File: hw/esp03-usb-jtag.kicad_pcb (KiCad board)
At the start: 2 copper layers, 92.7 x 55.9 mm, 45 parts, among them J1 USB, P1 JTAG, P2 SERIAL, P3 CONN_2, SW1 POWER/RESET, SW2 STRAP, U1 ESP8266-ESP03, U2 FT2232H, U3 LM1117, U4 93LC46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

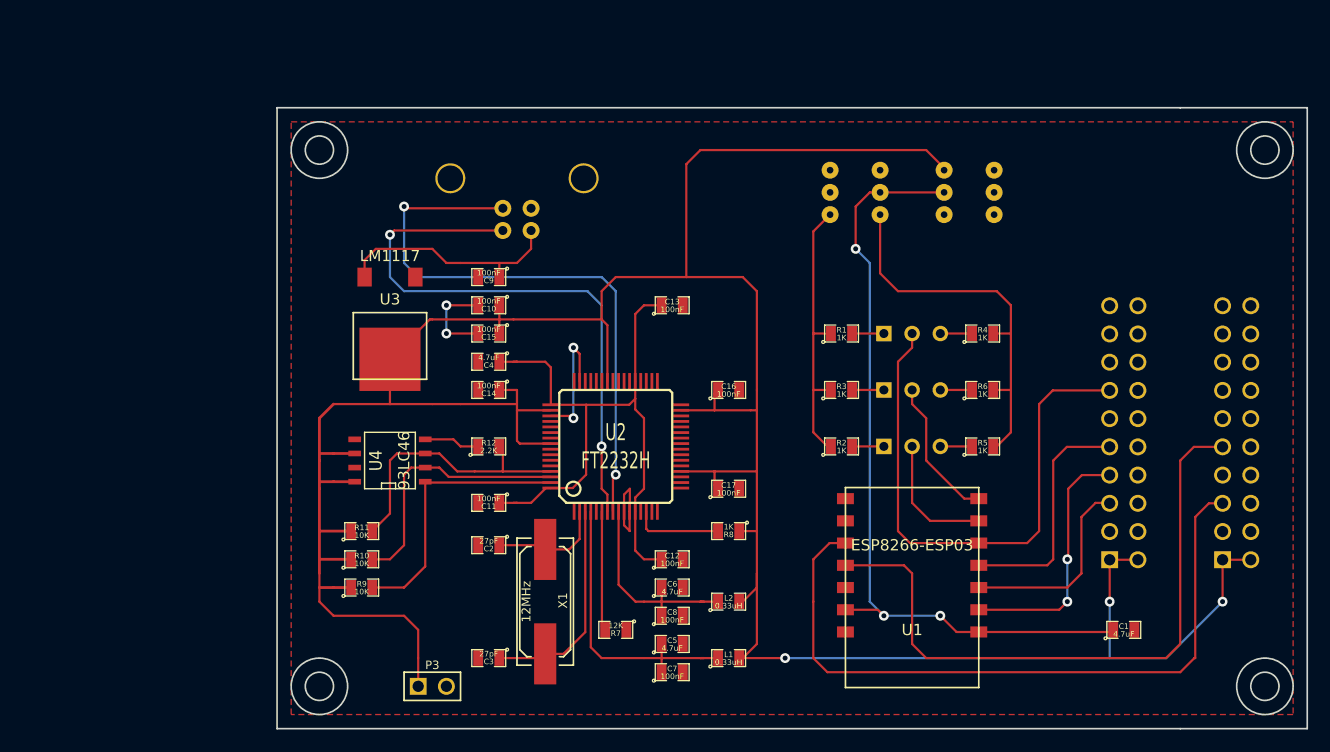
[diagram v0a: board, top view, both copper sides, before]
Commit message: hw: update PCB with FTDI JTAG and UART
Signed-off-by: Max Filippov <jcmvbkbc@gmail.com>
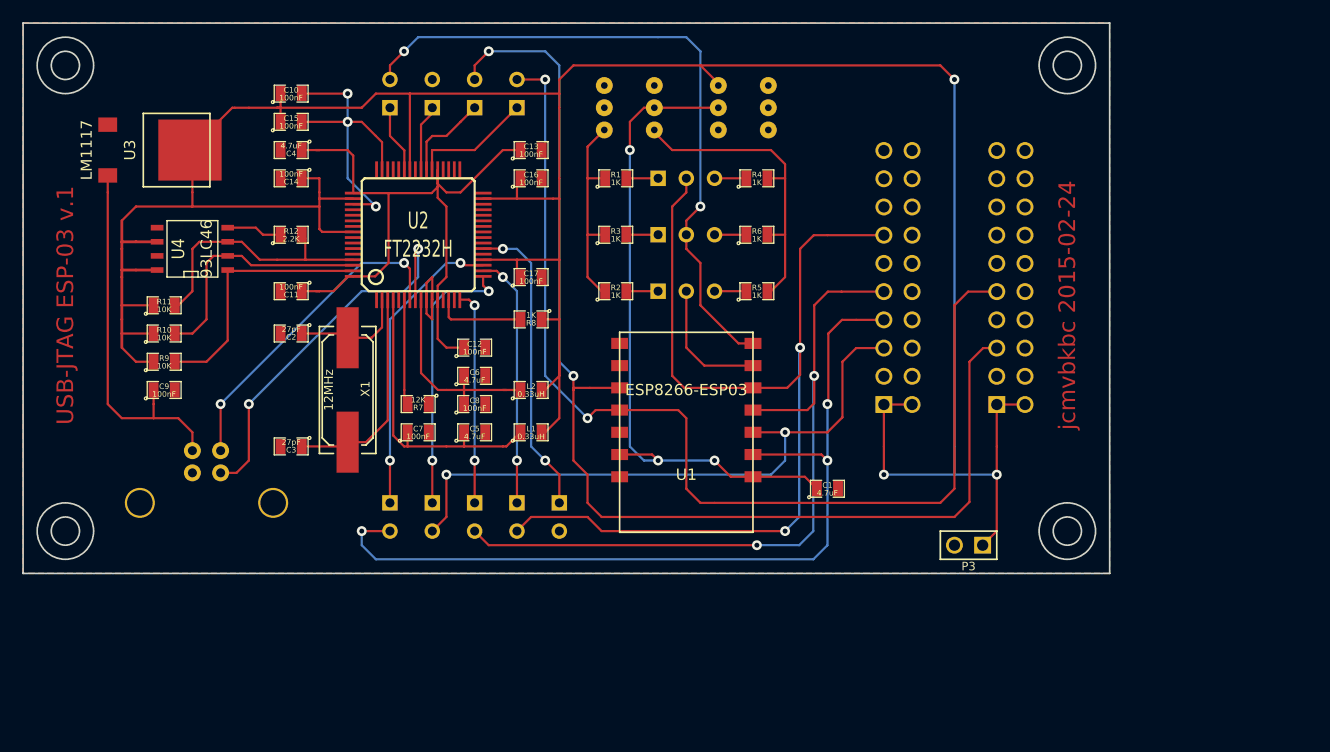
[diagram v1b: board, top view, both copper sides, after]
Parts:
- added JP10: JUMPER, SIL-2, B.Cu at (72.4, 36.8)
- added JP11: JUMPER, SIL-2, B.Cu at (68.6, 36.8)
- added JP12: JUMPER, SIL-2, B.Cu at (64.8, 36.8)
- added JP4: JUMPER, SIL-2, B.Cu at (64.8, 74.9)
- added JP5: JUMPER, SIL-2, B.Cu at (68.6, 74.9)
- added JP6: JUMPER, SIL-2, B.Cu at (72.4, 74.9)
- added JP7: JUMPER, SIL-2, B.Cu at (76.2, 74.9)
- added JP8: JUMPER, SIL-2, B.Cu at (80.0, 74.9)
- added JP9: JUMPER, SIL-2, B.Cu at (76.2, 36.8)
- moved P3 49.9 mm to (116.8, 77.5), turned to 180 degrees
- moved J1 40.4 mm to (48.3, 73.7), turned to 180 degrees
- moved C7 31.4 mm to (67.3, 67.3)
- moved C9 30.9 mm to (44.5, 63.5), turned to 0 degrees
- moved C1 29.5 mm to (104.1, 72.4)
- moved U3 27.9 mm to (39.4, 41.9), turned to 270 degrees
- moved R7 27.0 mm to (67.3, 64.8)
- moved R11 27.0 mm to (44.5, 55.9)
- moved R9 27.0 mm to (44.5, 61.0)
- moved L1 27.0 mm to (77.5, 67.3)
- moved R10 27.0 mm to (44.5, 58.4)
- moved C6 26.1 mm to (72.4, 62.2)
- moved R8 26.1 mm to (77.5, 57.1)
- moved C10 26.1 mm to (55.9, 36.8), turned to 0 degrees
- moved C12 26.1 mm to (72.4, 59.7)
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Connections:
- U2 pad 16: (no net) -> /FT_MTCK
- U2 pad 17: (no net) -> /FT_MTDI
- U2 pad 18: (no net) -> /FT_MTDO
- U2 pad 19: (no net) -> /FT_MTMS
- U2 pad 22: (no net) -> /FT_SRST
- U2 pad 38: (no net) -> /FT_TXD
- U2 pad 39: (no net) -> /FT_RXD
- U2 pad 40: (no net) -> /FT_RTS
- U2 pad 43: (no net) -> /FT_DTR
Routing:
- net /MTMS: track 22.7 -> 78.3 mm, vias 2 -> 3
- net /GPIO0: track 13.0 -> 60.9 mm, vias 0 -> 2
- net /MTCK: track 21.4 -> 66.9 mm, vias 0 -> 2
- net /RX: track 63.5 -> 105.9 mm, vias 0 -> 2
- net /MTDO: track 50.2 -> 92.4 mm, vias 0 -> 2
- net /MTDI: track 17.9 -> 57.0 mm, vias 0 -> 2
- net /TX: track 58.7 -> 96.5 mm, vias 0 -> 2
- net /FT_SRST: track 0.00 -> 27.5 mm, vias 0 -> 2
- net /FT_MTMS: track 0.00 -> 27.1 mm, vias 0 -> 2
- net /FT_MTDI: track 0.00 -> 24.9 mm, vias 0 -> 2
- net N-000006: track 53.0 -> 29.5 mm
- net /FT_MTDO: track 0.00 -> 22.9 mm, vias 0 -> 2
- net /FT_MTCK: track 0.00 -> 19.3 mm, vias 0 -> 2
- net N-000007: track 54.1 -> 35.3 mm
- net N-000005: track 20.9 -> 33.4 mm
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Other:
- board size 92.7 x 55.9 mm -> 97.8 x 49.5 mm
- board text added: "USB-JTAG ESP-03 v.1"
- board text added: "jcmvbkbc 2015-02-24"

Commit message: hw: usb-jtag: update JTAG and UART connectors location
Signed-off-by: Max Filippov <jcmvbkbc@gmail.com>
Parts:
- moved C17 150.3 mm to (227.3, 41.9)
- moved JP4 150.3 mm to (214.6, 63.5)
- moved JP5 150.3 mm to (218.4, 63.5)
- moved JP6 150.3 mm to (222.2, 63.5)
- moved JP7 150.3 mm to (226.1, 63.5)
- moved JP8 150.3 mm to (229.9, 63.5)
- moved C1 150.3 mm to (254.0, 61.0)
- moved C10 150.3 mm to (205.7, 25.4)
- moved C11 150.3 mm to (205.7, 43.2)
- moved C12 150.3 mm to (222.2, 48.3)
- moved C13 150.3 mm to (227.3, 30.5)
- moved C14 150.3 mm to (205.7, 33.0)
- moved C15 150.3 mm to (205.7, 27.9)
- moved C16 150.3 mm to (227.3, 33.0)
- moved C2 150.3 mm to (205.7, 47.0)
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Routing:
- net /TX: track 96.5 -> 95.1 mm
- net /MTDI: track 57.0 -> 55.7 mm
- net /MTMS: track 78.3 -> 77.0 mm
- net /MTDO: track 92.4 -> 91.1 mm
- net /MTCK: track 66.9 -> 65.6 mm
- net /RX: track 105.9 -> 104.7 mm
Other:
- outline, holes or cut-outs redrawn
- board text added: "USB-JTAG ESP-03 v.1.1"
- board text added: "jcmvbkbc 2015-02-26"
- board text removed: "USB-JTAG ESP-03 v.1"
- board text removed: "jcmvbkbc 2015-02-24"

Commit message: hw: invert the SRST signal, add it to PCB, update drawings
Signed-off-by: Max Filippov <jcmvbkbc@gmail.com>
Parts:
- added Q1: MMBT2222A, SOT23, F.Cu at (232.4, 47.0)
- added R13: 10K, SM0805, F.Cu at (227.3, 39.4)
- added R14: 47K, SM0805, F.Cu at (227.3, 36.8)
- added R15: 56, SM0805, F.Cu at (227.3, 58.4)
- moved C17 1.27 mm to (227.3, 43.2)
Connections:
- JP8 pad 1: /FT_SRST -> /SRST
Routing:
- net /FT_SRST: track 27.5 -> 3.38 mm, vias 2 -> 0
- net N-0000035: track 0.00 -> 13.0 mm
- net N-0000034: track 0.00 -> 12.1 mm
- net /SRST: track 0.00 -> 6.00 mm
- net +3.3V: track 271.9 -> 274.5 mm
- net /RX: track 104.7 -> 102.9 mm
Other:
- board text added: "USB-JTAG ESP-03 v.1.2"
- board text added: "jcmvbkbc 2015-02-28"
- board text removed: "USB-JTAG ESP-03 v.1.1"
- board text removed: "jcmvbkbc 2015-02-26"
